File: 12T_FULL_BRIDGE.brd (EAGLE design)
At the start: 49.4 x 55.2 mm, 49 parts

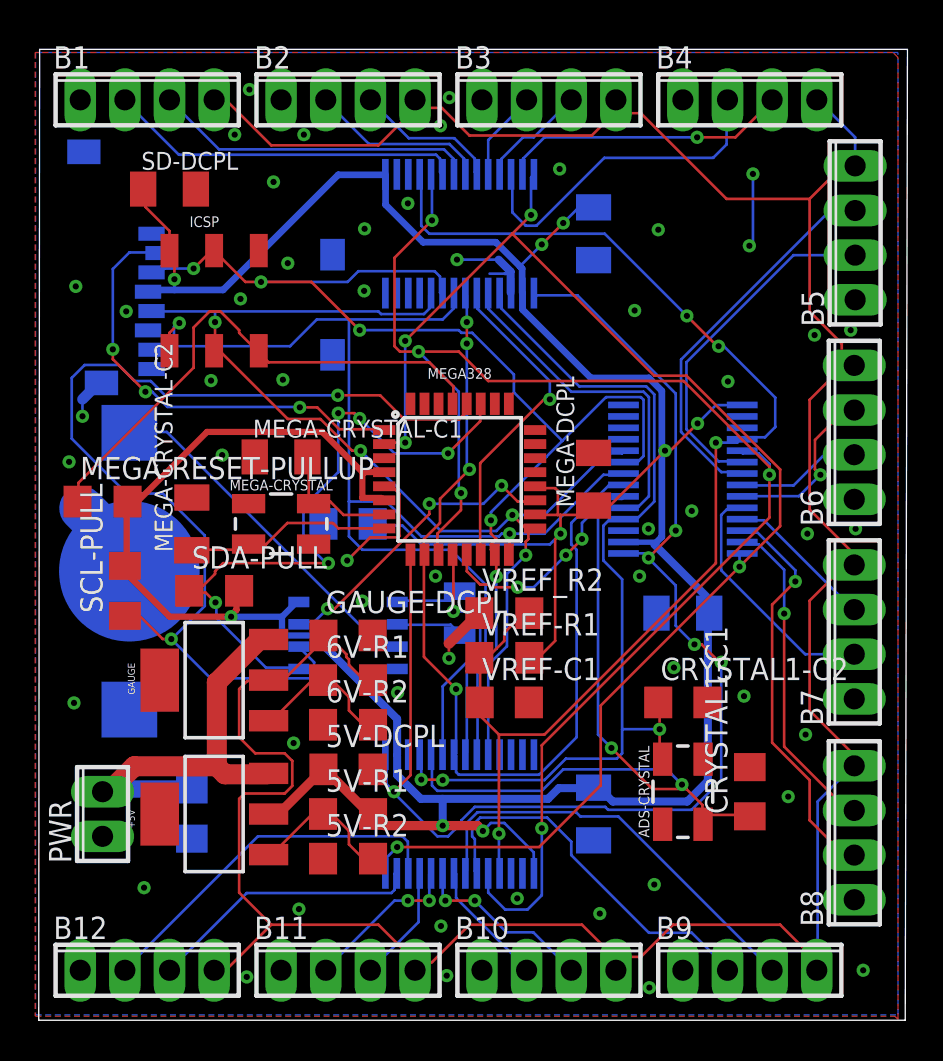
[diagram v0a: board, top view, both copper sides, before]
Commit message: Increased power trace width
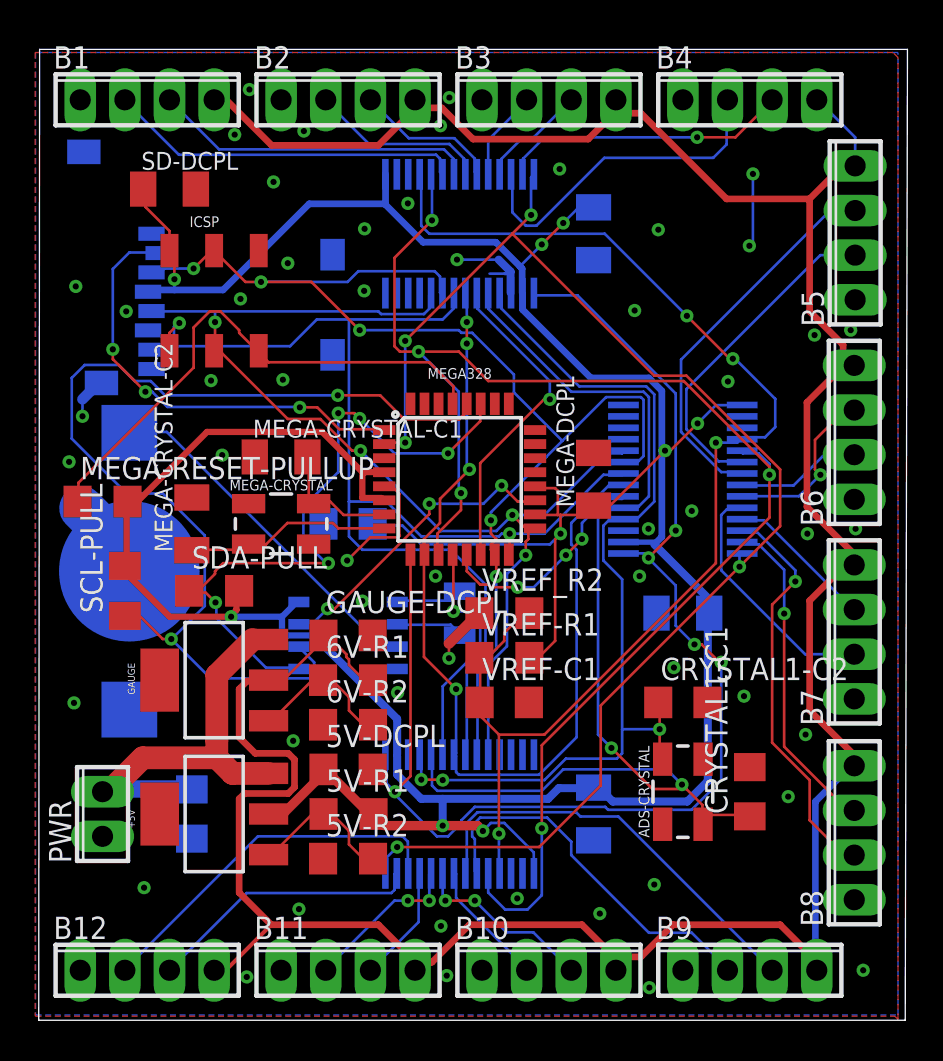
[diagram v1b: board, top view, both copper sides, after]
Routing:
- net +5V: track 205.6 -> 206.7 mm
- net B5-: track 19.9 -> 19.0 mm
- net VCC: track 173.4 -> 174.2 mm

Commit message: Ground plane, readability, trace length, yadda yadda yadda
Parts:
- moved 5V-R1 0.26 mm to (17.8, 12.4)
- renumbered CRYSTAL1-C1 to CRYS2-C1, CRYSTAL1-C2 to CRYS2-C2, GAUGE-DCPL to 6V-DCPL, MEGA-CRYSTAL-C1 to CRYS-C1, MEGA-CRYSTAL-C2 to CRYS-C2, MEGA-RESET-PULLUP to MEGA-RST-PULL, PWR-DCPL1 to PWR-DCPL
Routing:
- net GND: track 27.4 -> 32.2 mm, vias 52 -> 90
- net ADS-RESET: track 74.1 -> 74.7 mm
- net +5V: track 206.7 -> 206.1 mm
- net VCC: track 174.2 -> 173.7 mm
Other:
- board text added: "+"
- board text added: "-"
- board text added: "6V"
- board text added: "B+"
- board text added: "B-"
- board text added: "Designed by: Tony Sancho"
